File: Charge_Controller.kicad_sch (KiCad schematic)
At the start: 160 parts, among them J1 SOLAR, J10 Conn_01x01_Female, J11 Conn_01x01_Female, J12 Conn_01x01_Female, J13 Conn_01x01_Female, J14 Conn_01x01_Female, J15 Conn_01x01_Female, J16 Conn_01x01_Female, J17 Conn_01x01_Female, J18 Conn_01x01_Female, J19 Conn_01x01_Female, J2 Conn_01x01_Female, J20 Conn_01x01_Female, J21 Conn_01x01_Female, J22 Conn_01x01_Female, J23 Conn_01x01_Female, J24 Conn_01x01_Female, J25 Conn_01x01_Female, J26 Conn_01x01_Female, J27 Conn_01x01_Female, J28 Conn_01x01_Female, J29 Conn_01x01_Female, J3 Conn_01x01_Female, J30 Conn_01x01_Female, J31 Conn_01x01_Female, J32 Conn_01x01_Female, J33 Conn_01x01_Female, J34 Conn_01x01_Female, J36 FAN, J38 I2C_CON, J4 Conn_01x01_Female, J5 Conn_01x01_Female, J6 Conn_01x01_Female, J7 Conn_01x01_Female, J8 BATT, J9 USB_OTG, Q1 CSD19505, Q2 CSD19505, Q3 CSD19505, Q4 Si2306, Q5 2N3904, Q6 2N3904, Q7 PMOS-100V-78A, Q8 PMOS-100V-78A, Q9 Si2306, SW1 RIGHT, SW2 LEFT, SW3 BACK, SW4 SELECT, U1 Hall Amp Sense, U10 ADS1015, U11 NUP4202, U12 PCF8574, U2 B1212, U3 AMS1117-5.0, U4 AMS1117-3.3, U5 XL7005A, U6 XL7005A, U7 IR2104, U8 ESP32-WROOM-32, U9 CH340C

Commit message: Draft layout, still needs a bunch, but everything is connected.
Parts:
- added F1, F2: 25A, Symbol:ESD-Logo_6.6x6mm_SilkScreen, symbol Graphic:SYM_Arrow45_Small
- added L11: 7443783533650, 7443783533650_inductor:7443783533650, symbol 7443783533650_inductor:7443783533650
- C28: value 100nf -> 470nf; LCSC C28233 -> C13967
- H1: renamed from F1; value 35A -> Holder; footprint Fuse:Fuseholder_Blade_Mini_Keystone_3568 -> Fuse_Holder:Fuse_Blade_C2935871; Digikey 36-3568-10-ND -> (none); LCSC NA -> C2935871
- H2: renamed from F2; value 35A -> Holder; footprint Fuse:Fuseholder_Blade_Mini_Keystone_3568 -> Fuse_Holder:Fuse_Blade_C2935871; Digikey 36-3568-10-ND -> (none); LCSC NA -> C2935871
- HS1: value Heatsink -> 100x41x8mm Aluminum Heat Sink; footprint Heatsink:Heatsink_Stonecold_HS-132_32x14mm_2xFixation1.5mm -> MountingHole:MountingHole_2.5mm_Pad_Via; symbol Mechanical:Heatsink -> Mechanical:Heatsink_Pad; Digikey AE10798-ND -> NA
- J1, J36, J8: footprint Phoenix_10.16_terminal_1709681:Phoenix_10.16_terminal_1709681 -> TerminalBlock_MetzConnect:TerminalBlock_MetzConnect_Type703_RT10N02HGLU_1x02_P9.52mm_Horizontal; Digikey 277-13746-ND -> (none); LCSC NA -> C92145
- J33, J34: footprint TestPoint:TestPoint_Loop_D3.50mm_Drill0.9mm_Beaded -> MountingHole:MountingHole_2.5mm_Pad_Via
- Q1, Q2, Q3: footprint Package_TO_SOT_THT:TO-220-3_Vertical -> Package_TO_SOT_SMD:TO-263-2
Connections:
- net 3.3V is gone; now on net +3.3VA: C16.1, C17.1, J3.1 (Pin_1), L3.2, R17.1, R18.1
- net 12V: now also J36.2 (Pin_2); no longer J36.1 (Pin_1)
- net B+: now also J8.2 (Pin_2); no longer J8.1 (Pin_1)
- net B+Fused: now also L11.4
- net BuckFB: now also L11.1
- net GND: now also HS1.1, J8.1 (Pin_1); no longer J8.2 (Pin_2)
- net S+Fused2: now also U1.1 (IP+), U1.2 (IP+); no longer U1.3 (IP-), U1.4 (IP-)
- net S+Polarity: now also U1.3 (IP-), U1.4 (IP-); no longer U1.1 (IP+), U1.2 (IP+)
- net L2: now reaches LED2.2 (A), R6.1
- net at Q9.1 (D): now also J36.1 (Pin_1); no longer J36.2 (Pin_2)
- no-connect marks 2 -> 4
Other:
- note added: "65uH 20.7A"
- note added: "Optional manual wind L1"
- note added: "Q2 watts prediction W from Rds up to 2.6mohm * 35A^2 = 3W 16nS rise + 62nS fall = 78nS transition time per pulse At 39kHz that's 3mS of transition time per second. W from switching aprox 16nS +"
- note removed: "6 turns"
- moved on the sheet: C1, C2, C24, C9, D11, D12, D13, J36, J8, R1, R2, R3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

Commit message: R0.1 ready for review
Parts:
- C18: LCSC NA -> C503212
- D12, D13: value 120V-26A -> 90V-34A
- DS1: LCSC NA -> C83275
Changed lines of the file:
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@@
   (junction (at 42.545 55.88) (diameter 0) (color 0 0 0 0)
   )
-  (junction (at 100.33 55.88) (diameter 0) (color 0 0 0 0)
-  )
   (junction (at 32.385 33.02) (diameter 0) (color 0 0 0 0)
   )
@@
     (stroke (width 0) (type default) (color 0 0 0 0))
   )
-  (wire (pts (xy 100.33 57.785) (xy 100.33 55.88))
-    (stroke (width 0) (type default) (color 0 0 0 0))
-  )
   (wire (pts (xy 122.555 105.41) (xy 122.555 107.95))
     (stroke (width 0) (type default) (color 0 0 0 0))
@@
       (effects (font (size 1.27 1.27)) hide)
     )
-    (property "LCSC" "NA" (id 6) (at 19.05 64.135 0)
+    (property "LCSC" "C503212" (id 6) (at 19.05 64.135 0)
       (effects (font (size 1.27 1.27)) hide)
     )
@@
       (effects (font (size 1.27 1.27)) hide)
     )
-    (property "LCSC" "NA" (id 5) (at 300.355 151.13 0)
+    (property "LCSC" "C83275" (id 5) (at 300.355 151.13 0)
       (effects (font (size 1.27 1.27)) hide)
     )
@@
   (symbol (lib_id "power:+3.3VA") (at 73.66 25.4 0) (unit 1)
     (in_bom yes) (on_board yes)
-    (property "Reference" "#PWR?" (id 0) (at 73.66 29.21 0)
+    (property "Reference" "#PWR0102" (id 0) (at 73.66 29.21 0)
       (effects (font (size 1.27 1.27)) hide)
     )
@@
       (effects (font (size 1.27 1.27)) (justify right))
     )
-    (property "Value" "120V-26A" (id 1) (at 43.18 144.145 90)
+    (property "Value" "90V-34A" (id 1) (at 43.18 144.145 90)
       (effects (font (size 1.27 1.27)) (justify right) hide)
     )
@@
       (effects (font (size 1.27 1.27)) (justify right))
     )
-    (property "Value" "120V-26A" (id 1) (at 46.99 144.145 90)
+    (property "Value" "90V-34A" (id 1) (at 46.99 144.145 90)
       (effects (font (size 1.27 1.27)) (justify right) hide)
     )
@@
     )
     (path "/9301e6ff-9af4-4833-ac43-cf6bb26090e6"
-      (reference "#PWR?") (unit 1) (value "+3.3V") (footprint "")
+      (reference "#PWR0102") (unit 1) (value "+3.3V") (footprint "")
     )
     (path "/00000000-0000-0000-0000-0000634fa01d"
@@
     )
     (path "/adfe585e-a96d-48ad-83e2-afcc3c68924e"
-      (reference "D12") (unit 1) (value "120V-26A") (footprint "Diode_SMD:D_SMC-RM10_Universal_Handsoldering")
+      (reference "D12") (unit 1) (value "90V-34A") (footprint "Diode_SMD:D_SMC-RM10_Universal_Handsoldering")
     )
     (path "/b26990f5-9446-47f6-a5fb-c1fd9a39e041"
-      (reference "D13") (unit 1) (value "120V-26A") (footprint "Diode_SMD:D_SMC-RM10_Universal_Handsoldering")
+      (reference "D13") (unit 1) (value "90V-34A") (footprint "Diode_SMD:D_SMC-RM10_Universal_Handsoldering")
     )
     (path "/0f9e0af6-ba14-42c4-91ef-cf630523e014"

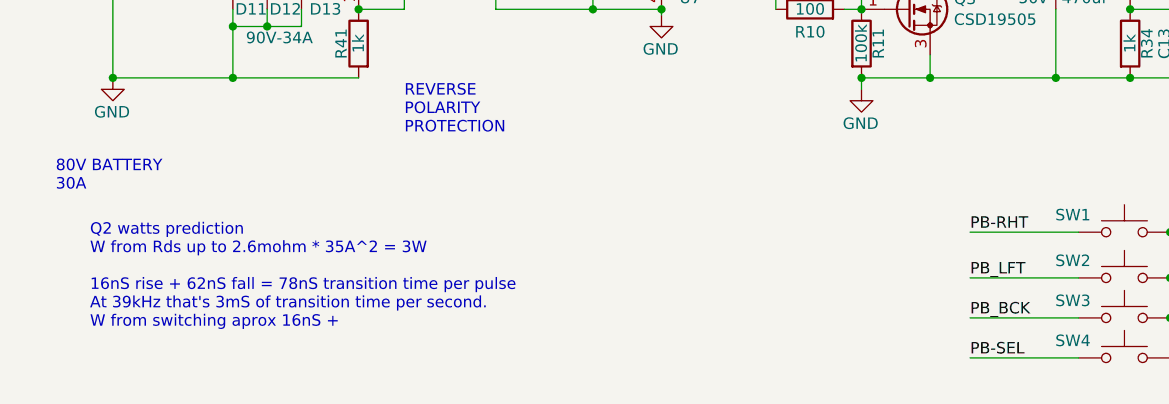
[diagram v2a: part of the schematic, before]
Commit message: Updated Q2 and Q3 watts prediction note on schematic. It now notes the spice simulation prediction watts.
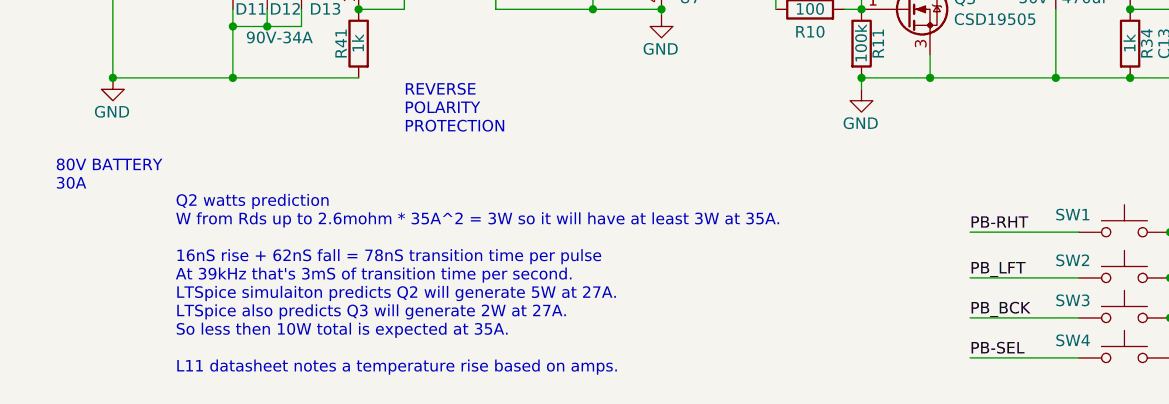
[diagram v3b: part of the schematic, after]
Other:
- note added: "Q2 watts prediction W from Rds up to 2.6mohm * 35A^2 = 3W so it will have at least 3W at 35A. 16nS rise + 62nS fall = 78nS transition time per pulse At 39kHz that's 3mS of transition time per second. LTSpice simulaiton predicts Q2 will generate 5W at 27A. LTSpice also predicts Q3 will generate 2W at 27A. So less then 10W total is expected at 35A. L11 datasheet notes a temperature rise based on am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"
- note removed: "Q2 watts prediction W from Rds up to 2.6mohm * 35A^2 = 3W 16nS rise + 62nS fall = 78nS transition time per pulse At 39kHz that's 3mS of transition time per second. W from switching aprox 16nS +"
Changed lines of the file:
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@@
     (effects (font (size 1.27 1.27)) (justify left bottom))
   )
-  (text "Q2 watts prediction\nW from Rds up to 2.6mohm * 35A^2 = 3W\n\n16nS rise + 62nS fall = 78nS transition time per pulse\nAt 39kHz that's 3mS of transition time per second. \nW from switching aprox 16nS +  "
-    (at 20.32 195.58 0)
+  (text "Q2 watts prediction\nW from Rds up to 2.6mohm * 35A^2 = 3W so it will have at least 3W at 35A.\n\n16nS rise + 62nS fall = 78nS transition time per pulse\nAt 39kHz that's 3mS of transition time per second. \nLTSpice simulaiton predicts Q2 will generate 5W at 27A.\nLTSpice also predicts Q3 will generate 2W at 27A.  \nSo less then 10W total is expected at 35A.\n\nL11 datasheet notes a temperature rise based on amps. "
+    (at 29.845 200.66 0)
     (effects (font (size 1.27 1.27)) (justify left bottom))
   )
